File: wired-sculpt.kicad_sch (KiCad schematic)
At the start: 39 parts, among them J1 10103594-0001LF, J2 FFC3B07-30-T, J3 AVR-ISP-6 - NOT FITTED, Q1 BSS84AK,215, Q2 2N7002BK, SW1 FSMSM, SW2 S2B-PH-K-S(LF)(SN), U1 USBLC6-2SC6, U2 LM2776DBVT, U3 AT90USB1286-AU, Y1 TSX-3225 16.0000MF18X-AC0

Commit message: Fix linkage of AT90 symbol
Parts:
- U3: symbol MCU_Microchip_AVR:AT90USB1286-AU -> MCU_Microchip_AVR:AT90USB1286-A
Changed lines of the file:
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@@
     )
   )
-  (symbol (lib_id "MCU_Microchip_AVR:AT90USB1286-AU") (at 140.97 86.36 0) (unit 1)
+  (symbol (lib_id "MCU_Microchip_AVR:AT90USB1286-A") (at 140.97 86.36 0) (unit 1)
     (in_bom yes) (on_board yes)
     (property "Reference" "U3" (id 0) (at 140.97 139.4206 0))

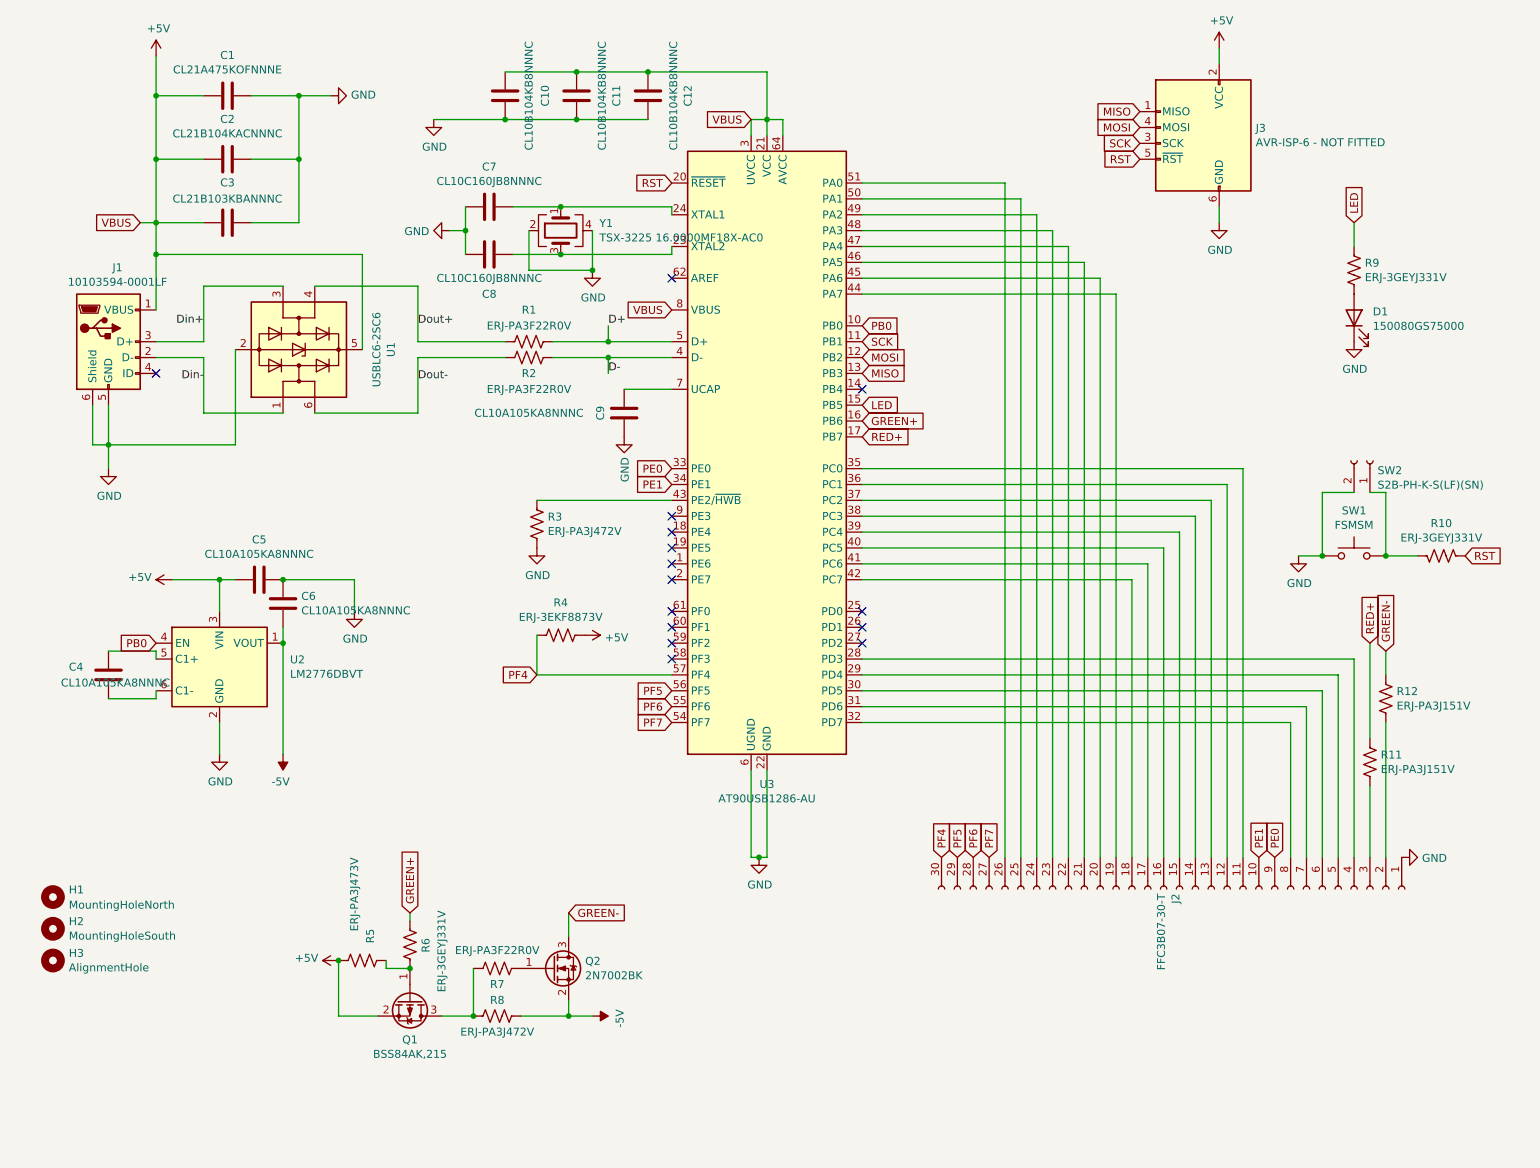
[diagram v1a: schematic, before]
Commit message: Add MPN to all components
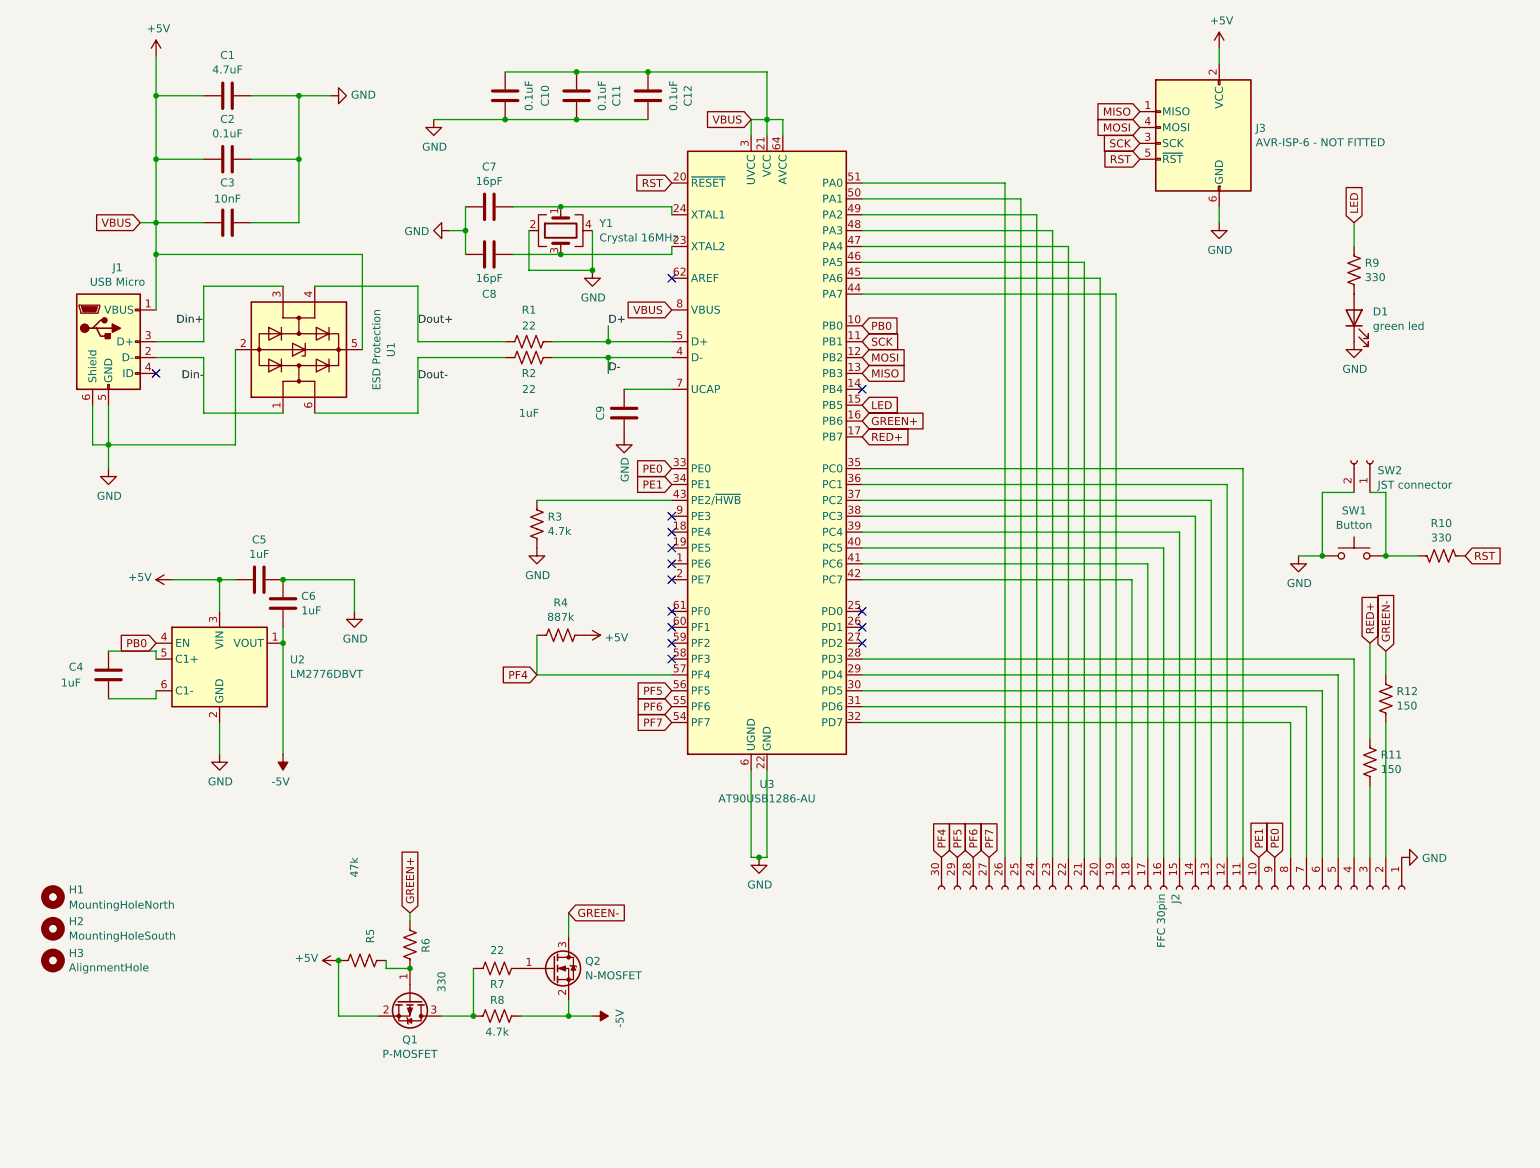
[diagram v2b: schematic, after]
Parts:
- C1: value CL21A475KOFNNNE -> 4.7uF; MPN (none) -> CL21A475KOFNNNE
- C10, C11, C12: value CL10B104KB8NNNC -> 0.1uF; MPN (none) -> CL10B104KB8NNNC
- C2: value CL21B104KACNNNC -> 0.1uF; MPN (none) -> CL21B104KACNNNC
- C3: value CL21B103KBANNNC -> 10nF; MPN (none) -> CL21B103KBANNNC
- C4, C5, C6, C9: value CL10A105KA8NNNC -> 1uF; MPN (none) -> CL10A105KA8NNNC
- C7, C8: value CL10C160JB8NNNC -> 16pF; MPN (none) -> CL10C160JB8NNNC
- D1: value 150080GS75000 -> green led; MPN (none) -> 150080GS75000
- J1: value 10103594-0001LF -> USB Micro; MPN (none) -> 10103594-0001LF
- J2: value FFC3B07-30-T -> FFC 30pin; MPN (none) -> FFC3B07-30-T
- J3: MPN (none) -> AVR-ISP-6 - NOT FITTED
- Q1: value BSS84AK,215 -> P-MOSFET; MPN (none) -> BSS84AK,215
- Q2: value 2N7002BK -> N-MOSFET; MPN (none) -> 2N7002BK
- R1, R2, R7: value ERJ-PA3F22R0V -> 22; MPN (none) -> ERJ-PA3F22R0V
- R10, R6, R9: value ERJ-3GEYJ331V -> 330; MPN (none) -> ERJ-3GEYJ331V
- R11, R12: value ERJ-PA3J151V -> 150; MPN (none) -> ERJ-PA3J151V
- R3, R8: value ERJ-PA3J472V -> 4.7k; MPN (none) -> ERJ-PA3J472V
- R4: value ERJ-3EKF8873V -> 887k; MPN (none) -> ERJ-3EKF8873V
- R5: value ERJ-PA3J473V -> 47k; MPN (none) -> ERJ-PA3J473V
- SW1: value FSMSM -> Button; MPN (none) -> FSMSM
- SW2: value S2B-PH-K-S(LF)(SN) -> JST connector; MPN (none) -> S2B-PH-K-S(LF)(SN)
- U1: value USBLC6-2SC6 -> ESD Protection; MPN (none) -> USBLC6-2SC6
- U2: MPN (none) -> LM2776DBVT
- U3: MPN (none) -> AT90USB1286-AU
- Y1: value TSX-3225 16.0000MF18X-AC0 -> Crystal 16MHz; MPN (none) -> TSX-3225 16.0000MF18X-AC0

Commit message: Copy MPN back to Value field
This is for compatbility with the JLCPCB plugin
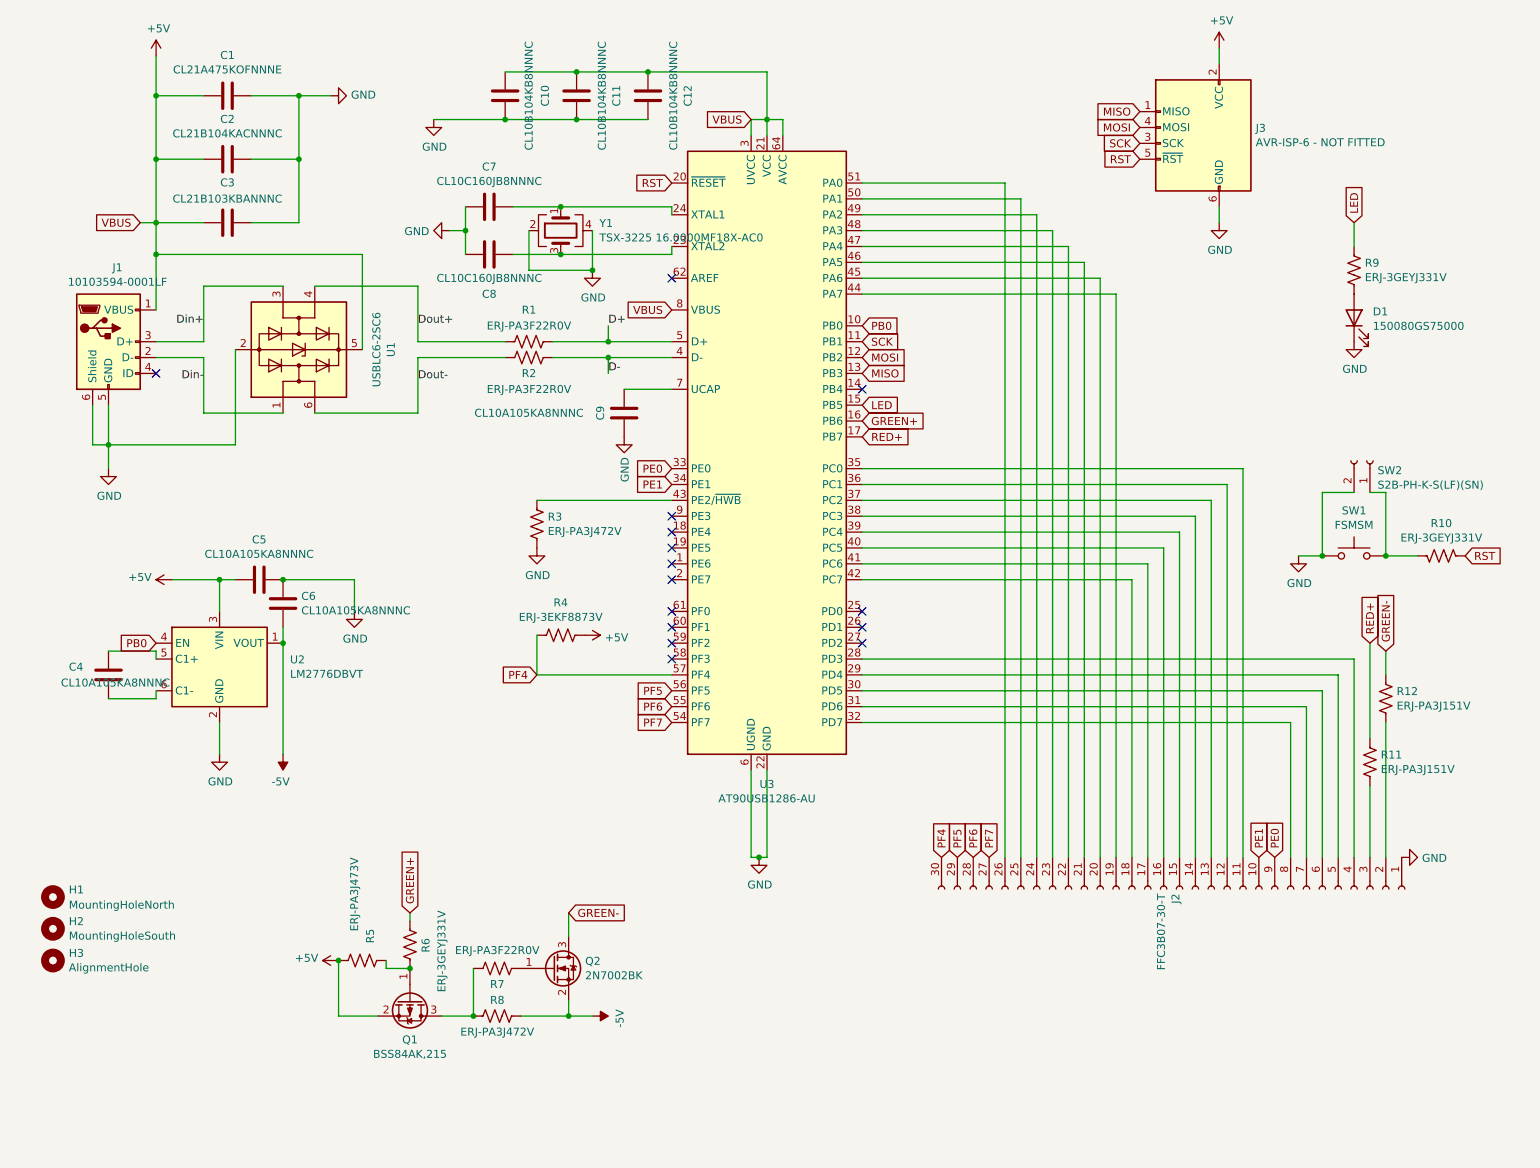
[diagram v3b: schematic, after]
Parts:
- C1: value 4.7uF -> CL21A475KOFNNNE; Notes (none) -> 4.7uF
- C10, C11, C12: value 0.1uF -> CL10B104KB8NNNC; Notes (none) -> 0.1uF
- C2: value 0.1uF -> CL21B104KACNNNC; Notes (none) -> 0.1uF
- C3: value 10nF -> CL21B103KBANNNC; Notes (none) -> 10nF
- C4, C5, C6, C9: value 1uF -> CL10A105KA8NNNC; Notes (none) -> 1uF
- C7, C8: value 16pF -> CL10C160JB8NNNC; Notes (none) -> 16pF
- D1: value green led -> 150080GS75000; Notes (none) -> green led
- J1: value USB Micro -> 10103594-0001LF; Notes (none) -> USB Micro port
- J2: value FFC 30pin -> FFC3B07-30-T; Notes (none) -> FFC 30pin
- Q1: value P-MOSFET -> BSS84AK,215; Notes (none) -> P-MOSFET
- Q2: value N-MOSFET -> 2N7002BK; Notes (none) -> N-MOSFET
- R1, R2, R7: value 22 -> ERJ-PA3F22R0V; Notes (none) -> 22Ohm
- R10, R6, R9: value 330 -> ERJ-3GEYJ331V; Notes (none) -> 330Ohm
- R11: value 150 -> ERJ-PA3J151V; Notes Allows 10 mA. Maybe 100R would be fine. -> 150Ohm
- R12: value 150 -> ERJ-PA3J151V; Notes Measures at 15-17 mA. -> 150Ohm
- R3, R8: value 4.7k -> ERJ-PA3J472V; Notes (none) -> 4.7kOhm
- R4: value 887k -> ERJ-3EKF8873V; Notes (none) -> 887kOhm
- R5: value 47k -> ERJ-PA3J473V; Notes (none) -> 47kOhm
- SW1: value Button -> FSMSM
- SW2: value JST connector -> S2B-PH-K-S(LF)(SN); Notes (none) -> JST connector
- U1: value ESD Protection -> USBLC6-2SC6; Notes (none) -> ESD Protection
- Y1: value Crystal 16MHz -> TSX-3225 16.0000MF18X-AC0; Notes (none) -> Crystal 16MHz

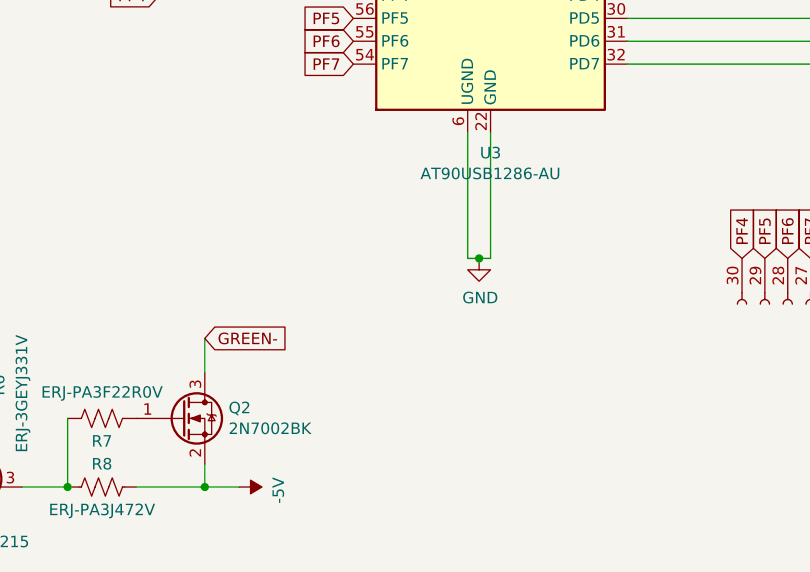
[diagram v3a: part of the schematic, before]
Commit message: Change microcontroller and one FET MPN
Fixes mismatch that PCBWay flagged
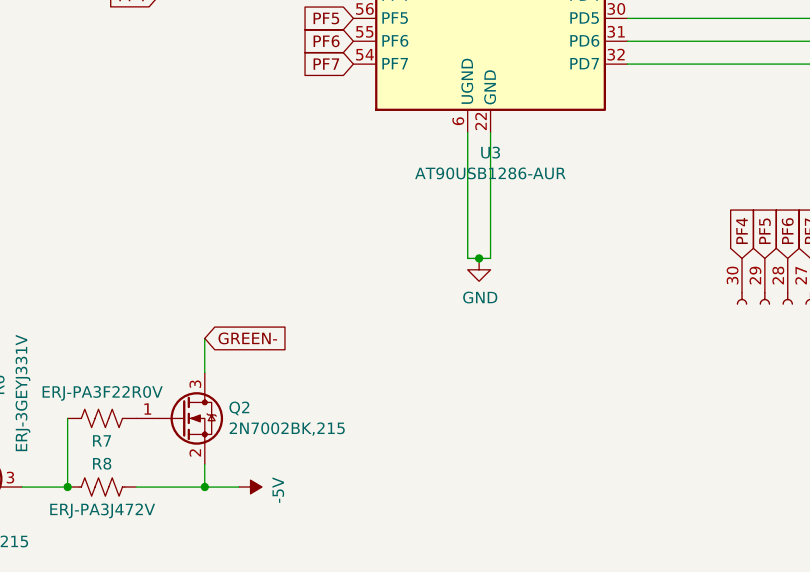
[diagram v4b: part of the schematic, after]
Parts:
- Q2: value 2N7002BK -> 2N7002BK,215; MPN 2N7002BK -> 2N7002BK,215
- U3: value AT90USB1286-AU -> AT90USB1286-AUR; MPN AT90USB1286-AU -> AT90USB1286-AUR
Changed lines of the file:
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@@
     (in_bom yes) (on_board yes)
     (property "Reference" "U3" (id 0) (at 140.97 139.4206 0))
-    (property "Value" "AT90USB1286-AU" (id 1) (at 140.97 141.732 0))
+    (property "Value" "AT90USB1286-AUR" (id 1) (at 140.97 141.732 0))
     (property "Footprint" "Package_QFP:TQFP-64_14x14mm_P0.8mm" (id 2) (at 140.97 86.36 0)
       (effects (font (size 1.27 1.27) italic) hide)
@@
       (effects (font (size 1.27 1.27)) hide)
     )
-    (property "MPN" "AT90USB1286-AU" (id 4) (at 140.97 86.36 0)
+    (property "MPN" "AT90USB1286-AUR" (id 4) (at 140.97 86.36 0)
       (effects (font (size 1.27 1.27)) hide)
     )
@@
       (effects (font (size 1.27 1.27)) (justify left))
     )
-    (property "Value" "2N7002BK" (id 1) (at 111.8616 170.053 0)
+    (property "Value" "2N7002BK,215" (id 1) (at 111.8616 170.053 0)
       (effects (font (size 1.27 1.27)) (justify left))
     )
@@
       (effects (font (size 1.27 1.27)) (justify left) hide)
     )
-    (property "MPN" "2N7002BK" (id 4) (at 106.68 168.91 0)
+    (property "MPN" "2N7002BK,215" (id 4) (at 106.68 168.91 0)
       (effects (font (size 1.27 1.27)) hide)
     )
@@
     )
     (path "/00000000-0000-0000-0000-0000607bf586"
-      (reference "Q2") (unit 1) (value "2N7002BK") (footprint "Package_TO_SOT_SMD:SOT-23")
+      (reference "Q2") (unit 1) (value "2N7002BK,215") (footprint "Package_TO_SOT_SMD:SOT-23")
     )
     (path "/00000000-0000-0000-0000-00005fc254cd"
@@
     )
     (path "/00000000-0000-0000-0000-00005fc15265"
-      (reference "U3") (unit 1) (value "AT90USB1286-AU") (footprint "Package_QFP:TQFP-64_14x14mm_P0.8mm")
+      (reference "U3") (unit 1) (value "AT90USB1286-AUR") (footprint "Package_QFP:TQFP-64_14x14mm_P0.8mm")
     )
     (path "/00000000-0000-0000-0000-00005fe44873"

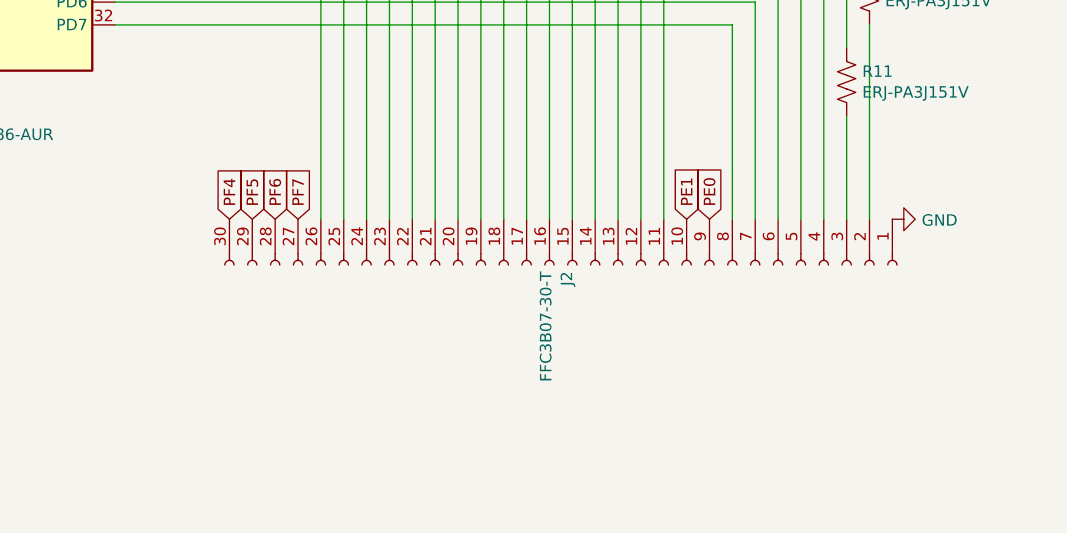
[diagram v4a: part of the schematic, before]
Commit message: Properly ground mounting pads for FFC
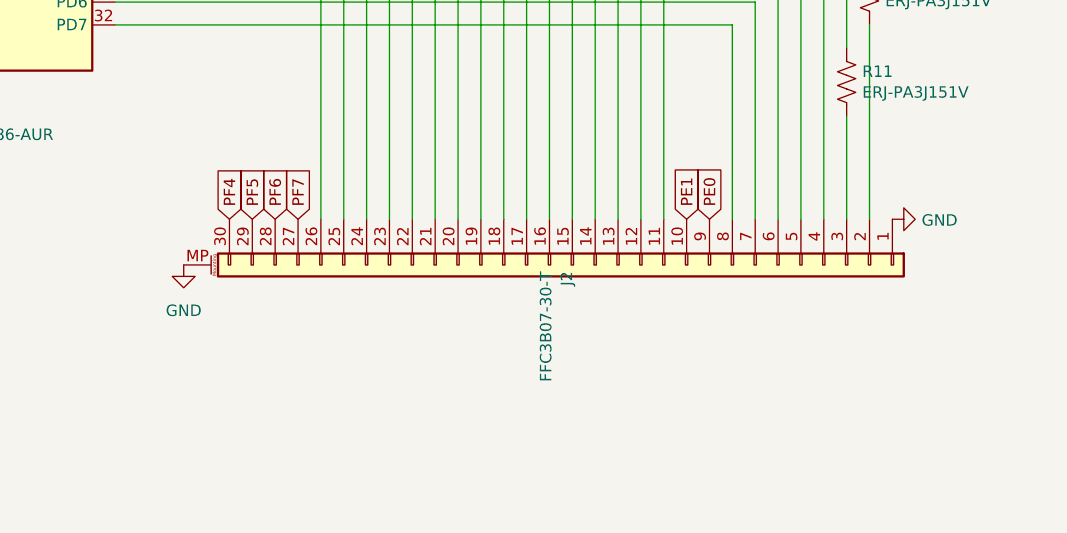
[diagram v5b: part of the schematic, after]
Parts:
- J2: symbol Connector:Conn_01x30_Female -> Connector_Generic_MountingPin:Conn_01x30_MountingPin
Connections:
- net GND: now also J2.MP (MountPin)
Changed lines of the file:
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@@
     (pin "2")
   )
-  (symbol (lib_id "Connector:Conn_01x30_Female") (at 207.01 156.21 270) (unit 1)
+  (symbol (lib_id "Connector_Generic_MountingPin:Conn_01x30_MountingPin") (at 207.01 156.21 270) (unit 1)
     (in_bom yes) (on_board yes)
     (property "Reference" "J2" (id 0) (at 206.4004 156.9212 0)
@@
     (pin "8")
     (pin "9")
+    (pin "MP")
   )
   (symbol (lib_id "Mechanical:MountingHole") (at 26.67 157.48 0) (unit 1)
@@
     (pin "2")
   )
+  (symbol (lib_id "power:GND") (at 163.83 156.21 0) (unit 1)
+    (in_bom yes) (on_board yes) (fields_autoplaced)
+    (property "Reference" "#PWR0101" (id 0) (at 163.83 162.56 0)
+      (effects (font (size 1.27 1.27)) hide)
+    )
+    (property "Value" "GND" (id 1) (at 163.83 161.29 0))
+    (property "Footprint" "" (id 2) (at 163.83 156.21 0)
+      (effects (font (size 1.27 1.27)) hide)
+    )
+    (property "Datasheet" "" (id 3) (at 163.83 156.21 0)
+      (effects (font (size 1.27 1.27)) hide)
+    )
+    (pin "1")
+  )
   (sheet_instances
     (path "/" (page "1"))
@@
       (reference "#PWR021") (unit 1) (value "-5V") (footprint "")
     )
+    (path "/8b1506f8-ccbc-40e9-b834-ee5190517a5d"
+      (reference "#PWR0101") (unit 1) (value "GND") (footprint "")
+    )
     (path "/00000000-0000-0000-0000-00005fc4ef1f"
